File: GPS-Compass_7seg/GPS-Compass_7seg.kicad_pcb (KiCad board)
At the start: 2 copper layers, 50.3 x 20.5 mm, 8 parts, among them J1 1-2328702-0, U1 OSK3056A-LR, U2 MAX7219

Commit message: GNSS and Mian ocb
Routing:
- net GND: track 4.96 -> 4.60 mm, vias 7 -> 50

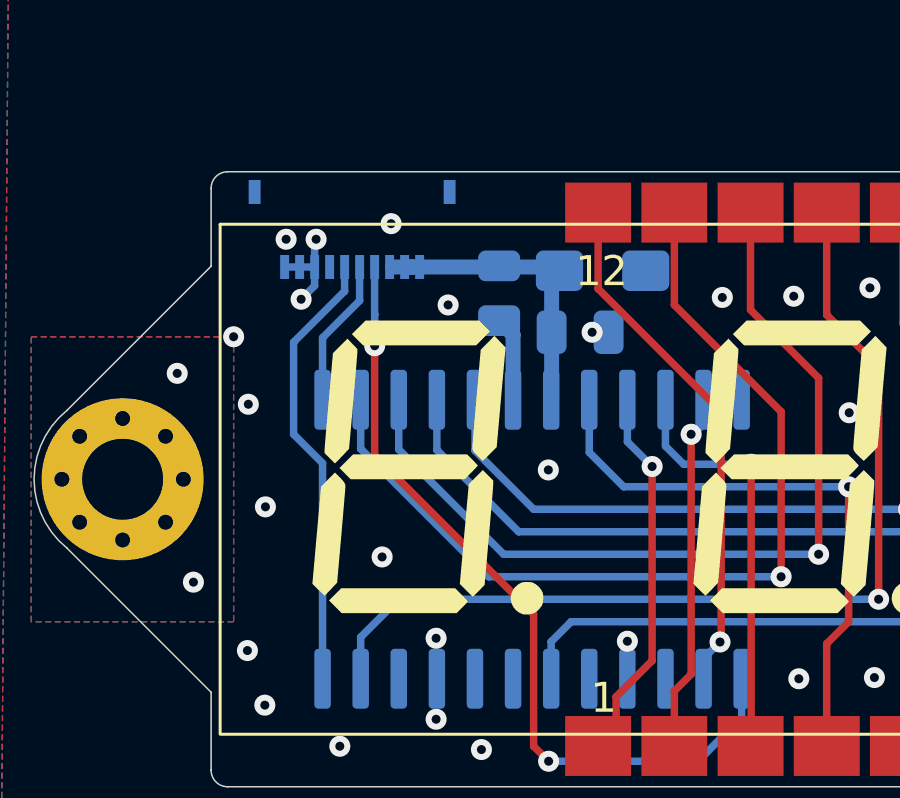
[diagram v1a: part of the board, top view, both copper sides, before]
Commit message: UI layout and routing
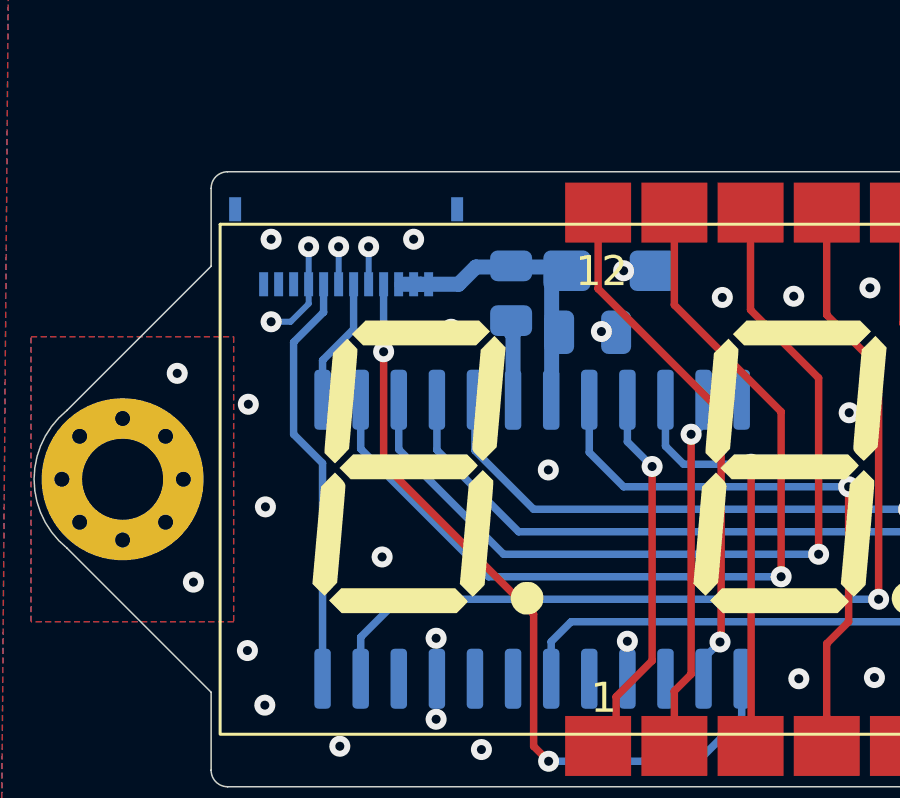
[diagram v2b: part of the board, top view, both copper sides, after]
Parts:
- removed J1: 1-2328702-0, gps-compass_brd:TE_1-2328702-0
- added G***: LOGO, sumec_graphic:COLON_3_IMG, B.Cu at (219.2, 64.5)
- added J2: FFC2B28-12-G, gps-compass_brd:GCT_FFC2B28-12-G, B.Cu at (193.0, 53.8)
- moved R1 0.40 mm to (198.5, 55.3)
- moved C1 0.25 mm to (201.8, 54.5)
- moved C2 0.25 mm to (201.1, 56.6)
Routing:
- net GND: track 4.60 -> 7.37 mm, vias 50 -> 52
- net ~{CS}: track 14.8 -> 14.0 mm
- net MOSI: track 27.2 -> 26.5 mm
- net CLK: track 4.94 -> 4.28 mm
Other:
- board text added: "0.5mm 12P"
- board text removed: "0.5mm 10P"

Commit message: changes s
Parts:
- C1: footprint Capacitor_Tantalum_SMD:CP_EIA-3216-18_Kemet-A_Pad1.58x1.35mm_HandSolder -> Capacitor_SMD:C_0805_2012Metric
- moved J2 14.8 mm to (207.8, 53.2)
- moved R1 2.33 mm to (196.5, 56.5), turned to 180 degrees
- moved C1 1.82 mm to (200.0, 54.2), turned to 180 degrees
- moved C2 1.05 mm to (200.0, 56.5), turned to 180 degrees
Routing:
- net CLK: track 4.28 -> 19.4 mm, vias 0 -> 2
- net ~{CS}: track 14.0 -> 27.8 mm, vias 0 -> 2
- net +5V: track 10.2 -> 21.8 mm
- net MOSI: track 26.5 -> 18.3 mm
- net DIG_2: track 28.6 -> 26.7 mm
- net Net-(U2-ISET): track 2.83 -> 4.54 mm, vias 0 -> 2
- net DIG_1: track 32.8 -> 31.4 mm
- net SEG_C: track 19.8 -> 18.8 mm
- net SEG_B: track 31.3 -> 30.3 mm
- net GND: track 7.37 -> 6.37 mm, vias 52 -> 43
- net SEG_G: track 24.9 -> 24.2 mm
- net SEG_F: track 29.4 -> 28.7 mm
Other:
- board text added: "5V"
